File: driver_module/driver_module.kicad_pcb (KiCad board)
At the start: 4 copper layers, 68.8 x 36 mm, 119 parts, among them J1 Power Input, J19 Conn_01x03, J2 Power Input, J21 Power Input, J4 Conn_02x06_Odd_Even, J5 Conn_02x06_Odd_Even, J6 Conn_01x06, Q1 Q_PNP_BEC, Q2 Q_PNP_BEC, Q3 Q_PNP_BEC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

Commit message: First pass responding to design review. Copper changes done but final review not complete.
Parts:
- removed the G*** at (144.9, 72.0)
- removed the G*** at (141.1, 59.7)
- removed the G*** at (142.9, 48.8)
- added C5: 2.2uF 100V, Capacitor_SMD:C_0805_2012Metric, B.Cu at (118.8, 102.9)
- added C7: DNP, Capacitor_SMD:C_0603_1608Metric, B.Cu at (119.0, 96.7)
- added C8: 4.7uF 35V, Capacitor_SMD:C_0603_1608Metric, B.Cu at (116.3, 102.8)
- added R10: R, Capacitor_SMD:C_0603_1608Metric, B.Cu at (115.7, 96.7)
- added R6: R, Capacitor_SMD:C_0603_1608Metric, B.Cu at (114.9, 102.7)
- added U3: TPS7A1601DGNT, parts:DGN0008C_N, B.Cu at (117.4, 99.4)
- moved J19 1.00 mm to (124.7, 100.0)
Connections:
- J4 pad 1: VMOT -> GND
- J4 pad 2: GND -> VMOT
- J4 pad 3: VMOT -> /M2A_P
- J4 pad 4: /M2A_P -> VMOT
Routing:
- net +12V: track 90.2 -> 126.9 mm, vias 0 -> 1
- net GND: track 75.1 -> 90.1 mm, vias 141 -> 136
- net VMOT: track 43.2 -> 52.6 mm
- net Net-(U3-FB): track 0.00 -> 6.95 mm
- net Net-(U3-DELAY): track 0.00 -> 4.33 mm
- net /M2A_P: track 34.0 -> 35.9 mm
- removed copper zone on F.Cu, net (none)
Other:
- board text removed: "0"
- board text removed: "1"
- board text removed: "A1"
- board text removed: "A2"
- board text removed: "ADC1"
- board text removed: "AUX1"
- board text removed: "AUX2"
- board text removed: "B1"
- board text removed: "B2"
- board text removed: "BOOT1"
- board text removed: "BOOT2"
- board text removed: "C"
- board text removed: "C1"
- board text removed: "C2"
- board text removed: "CAN INPUT"
- board text removed: "CAN OUTPUT"
- board text removed: "CAN2"
- board text removed: "CPU1/MOT"
- board text removed: "CPU2/AUX"
- board text removed: "Debug1"
- board text removed: "Debug2"
- board text removed: "Dual RP2040 BLDC Driver"
- board text removed: "ENA"
- board text removed: "ESTOP"
- board text removed: "PWR"
- board text removed: "Profile"
- board text removed: "REMOTE"
- board text removed: "RX"
- board text removed: "TX"
- board text removed: "USB1"
- board text removed: "USB2"
- board text removed: "on"

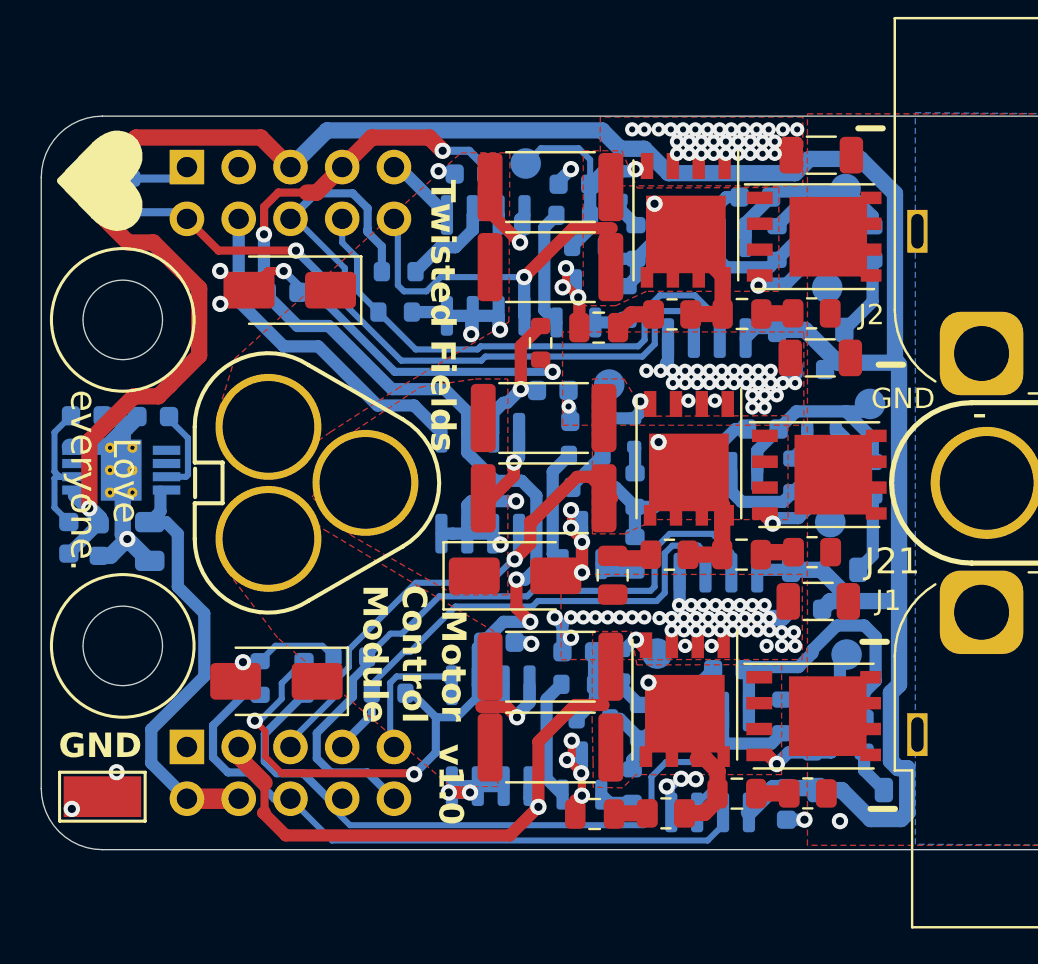
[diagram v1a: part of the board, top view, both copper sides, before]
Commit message: Clean up of motor, base, and UI PCBs. Could be ready to order.
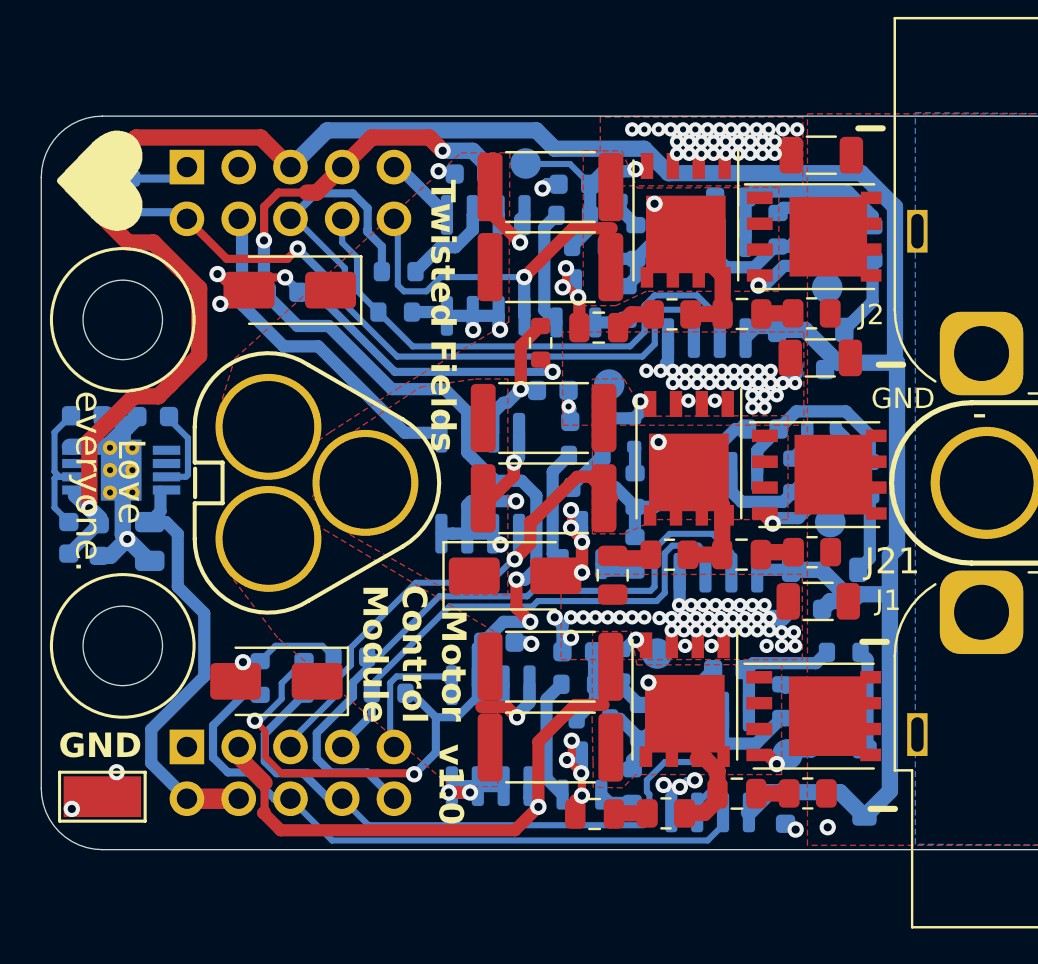
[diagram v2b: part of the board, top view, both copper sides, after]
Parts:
- removed TP62, TP78: TestPoint, parts:TestPoint_Pad_D1.5mm_no_courtyard
- C3, C6: value 150uF 63V solid -> 220uF 63V solid
- moved TP73 5.69 mm to (150.1, 113.3)
- moved R3 4.17 mm to (152.9, 108.3), turned to 180 degrees
- moved R33 1.21 mm to (152.2, 111.5), turned to 0 degrees
- moved C65 1.20 mm to (147.3, 86.0)
- moved D7 0.78 mm to (153.9, 114.7), turned to -90 degrees
- moved R31 0.75 mm to (149.8, 110.7)
- moved R8 0.65 mm to (149.7, 87.6)
- moved C15 0.21 mm to (150.0, 116.0)
- moved R26 0.15 mm to (154.2, 99.8)
- moved D17 0.11 mm to (151.9, 110.0)
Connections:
- net /M2A_N renamed /A_N
- net /M2A_P renamed /A_P
- net /M2B_N renamed /B_N
- net /M2B_P renamed /B_P
- net /M2C_N renamed /C_N
- net /M2C_P renamed /C_P
- net M2A_PWM_H renamed A_PWM_H
- net M2A_PWM_L\ renamed A_PWM_L\
- net M2A_SENSE renamed A_SENSE
- net M2B_PWM_H renamed B_PWM_H
- net M2B_PWM_L\ renamed B_PWM_L\
- net M2B_SENSE renamed B_SENSE
- net M2C_PWM_H renamed C_PWM_H
- net M2C_PWM_L\ renamed C_PWM_L\
- net M2C_SENSE renamed C_SENSE
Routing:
- net Net-(U8-VB): track 13.8 -> 6.30 mm
- net +12V: track 126.9 -> 123.3 mm
- net Net-(D7-K): track 2.29 -> 4.96 mm
- net /2AGH: track 9.04 -> 6.98 mm
- net Net-(U5-VB): track 10.6 -> 9.16 mm
- net /2CGL: track 11.5 -> 10.2 mm
- net GND: track 90.1 -> 88.8 mm
- net /C_P: track 29.8 -> 28.7 mm
- net A_PWM_L\: track 33.1 -> 32.5 mm
- net Net-(U2-VB): track 8.69 -> 9.29 mm
- net /TH1_SENSE: track 26.0 -> 26.5 mm
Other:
- board text added: "A"
- board text added: "B"
- board text added: "C"
- board text added: "H"
- board text added: "L"

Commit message: Respond to latest round of design review.
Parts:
- added D1: SMAJ51A, Diode_SMD:D_SMC, B.Cu at (163.2, 112.1)
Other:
- board text added: "github.com/ Twisted-Fields/rp2040-motor-controller"
- board text removed: "github.com/ Twisted-Fields/ rp2040-motor-controller"
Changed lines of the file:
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@@
     )
   )
+  (footprint "Diode_SMD:D_SMC" (layer "B.Cu")
+    (at 163.22 112.125 180)
+    (descr "Diode SMC (DO-214AB)")
+    (tags "Diode SMC (DO-214AB)")
+    (property "LCSC" "C438169")
+    (property "Sheetfile" "driver_module.kicad_sch")
+    (property "Sheetname" "")
+    (property "ki_description" "200W unidirectional Transil Transient Voltage Suppressor, 54Vrwm, SMF")
+    (property "ki_keywords" "diode TVS voltage suppressor")
+    (attr smd)
+    (fp_text reference "D1" (at 0 4.1) (layer "B.SilkS") hide
+        (effects (font (size 1 1) (thickness 0.15)) (justify mirror))
+    )
+    (fp_text value "SMAJ51A" (at 0 -4.2) (layer "B.Fab")
+        (effects (font (size 1 1) (thickness 0.15)) (justify mirror))
+    )
+    (fp_text user "${REFERENCE}" (at 0 1.9) (layer "B.Fab")
+        (effects (font (size 1 1) (thickness 0.15)) (justify mirror))
+    )
+    (fp_line (start -4.91 -3.25) (end -4.91 3.25)
+      (stroke (width 0.12) (type solid)) (layer "B.SilkS"))
+    (fp_line (start -4.91 -3.25) (end 3.6 -3.25)
+      (stroke (width 0.12) (type solid)) (layer "B.SilkS"))
+    (fp_line (start -4.91 3.25) (end 3.6 3.25)
+      (stroke (width 0.12) (type solid)) (layer "B.SilkS"))
+    (fp_line (start -4.9 -3.35) (end -4.9 3.35)
+      (stroke (width 0.05) (type solid)) (layer "B.CrtYd"))
+    (fp_line (start -4.9 3.35) (end 4.9 3.35)
+      (stroke (width 0.05) (type solid)) (layer "B.CrtYd"))
+    (fp_line (start 4.9 -3.35) (end -4.9 -3.35)
+      (stroke (width 0.05) (type solid)) (layer "B.CrtYd"))
+    (fp_line (start 4.9 3.35) (end 4.9 -3.35)
+      (stroke (width 0.05) (type solid)) (layer "B.CrtYd"))
+    (fp_line (start -3.55 -3.1) (end -3.55 3.1)
+      (stroke (width 0.1) (type solid)) (layer "B.Fab"))
+    (fp_line (start -0.64944 -0.00102) (end -1.55114 -0.00102)
+      (stroke (width 0.1) (type solid)) (layer "B.Fab"))
+    (fp_line (start -0.64944 -0.00102) (end 0.50118 -0.75032)
+      (stroke (width 0.1) (type solid)) (layer "B.Fab"))
+    (fp_line (start -0.64944 -0.00102) (end 0.50118 0.79908)
+      (stroke (width 0.1) (type solid)) (layer "B.Fab"))
+    (fp_line (start -0.64944 0.79908) (end -0.64944 -0.80112)
+      (stroke (width 0.1) (type solid)) (layer "B.Fab"))
+    (fp_line (start 0.50118 -0.75032) (end 0.50118 0.79908)
+      (stroke (width 0.1) (type solid)) (layer "B.Fab"))
+    (fp_line (start 0.50118 -0.00102) (end 1.4994 -0.00102)
+      (stroke (width 0.1) (type solid)) (layer "B.Fab"))
+    (fp_line (start 3.55 -3.1) (end -3.55 -3.1)
+      (stroke (width 0.1) (type solid)) (layer "B.Fab"))
+    (fp_line (start 3.55 3.1) (end -3.55 3.1)
+      (stroke (width 0.1) (type solid)) (layer "B.Fab"))
+    (fp_line (start 3.55 3.1) (end 3.55 -3.1)
+      (stroke (width 0.1) (type solid)) (layer "B.Fab"))
+    (pad "1" smd roundrect (at -3.4 0 90) (size 3.3 2.5) (layers "B.Cu" "B.Paste" "B.Mask") (roundrect_rratio 0.1)
+      (net 4 "VMOT") (pinfunction "A1") (pintype "passive"))
+    (pad "2" smd roundrect (at 3.4 0 90) (size 3.3 2.5) (layers "B.Cu" "B.Paste" "B.Mask") (roundrect_rratio 0.1)
+      (net 1 "GND") (pinfunction "A2") (pintype "passive"))
+    (model "${KICAD6_3DMODEL_DIR}/Diode_SMD.3dshapes/D_SMC.wrl"
+      (offset (xyz 0 0 0))
+      (scale (xyz 1 1 1))
+      (rotate (xyz 0 0 0))
+    )
+  )
   (footprint "Resistor_SMD:R_0603_1608Metric" (layer "B.Cu")
     (at 142.251268 91.17005 -90)
@@
         (effects (font (size 1 1) (thickness 0.15)) (justify mirror))
     )
+    (fp_text user "${REFERENCE}" (at -1.5 2.75 180 unlocked) (layer "B.SilkS")
+        (effects (font (size 1 1) (thickness 0.15)) (justify mirror))
+    )
     (fp_poly
       (pts
@@
     (effects (font (size 1 1) (thickness 0.15)) (justify mirror))
   )
-  (gr_text "      github.com/\n      Twisted-Fields/\nrp2040-motor-controller" (at 165.8 114.45) (layer "B.SilkS")
-    (effects (font (size 1 1) (thickness 0.2)) (justify mirror))
+  (gr_text "github.com/\nTwisted-Fields/rp2040-motor-controller" (at 180.8 115.95) (layer "B.SilkS")
+    (effects (font (size 0.8 0.8) (thickness 0.2)) (justify left mirror))
   )
   (gr_text "GND" (at 394.775 92.1) (layer "B.SilkS")

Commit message: Update boards for latest build, pending design review.
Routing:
- net +12V: track 123.3 -> 120.5 mm

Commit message: Change enable behavior and ensure low side FETs activate for hardware braking
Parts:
- removed G***: LOGO, taylor_footprints:twisted_2
- removed G***: LOGO, taylor_footprints:twisted_icon
- removed G***: LOGO, taylor_footprints:twisted
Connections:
- R119 pad 1: +3V3 -> GND
- R122 pad 1: +3V3 -> GND
- R124 pad 1: +3V3 -> GND
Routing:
- net +3V3: track 87.7 -> 61.7 mm, vias 7 -> 5
- net GND: track 88.8 -> 98.5 mm
- net /C_P: track 28.7 -> 26.4 mm
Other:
- board text added: "Love"
- board text added: "everyone."
- board text removed: "5V ISO"
- board text removed: "Designed by Sequoia Sempervirens For Twisted Fields"
- board text removed: "Dual CPU Version 3.2"
- board text removed: "ENC1"
- board text removed: "ENC2"
- board text removed: "Enc1 Filt"
- board text removed: "Enc2 Filt"
- board text removed: "GND ISO"
- board text removed: "Love everyone."
- board text removed: "Please clone this board!"
- board text removed: "RP2040 Brushless Motor Controller"
- board text removed: "The smallest change can be the beginning of something big."
- board text removed: "VMOT"
- board text removed: "We are all star stuff."
- board text removed: "We need your help. Fork the design and make it yours."
- board text removed: "You can do it!"

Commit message: Updated files for boards ordered July 2024
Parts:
- D1: value SMAJ51A -> SMDJ51CA
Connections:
- U3 pad 5: unconnected-(U3-EN-Pad5) -> VMOT
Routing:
- net VMOT: track 52.1 -> 56.7 mm, vias 1 -> 3
- net Net-(U3-DELAY): track 4.33 -> 5.13 mm
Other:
- board text added: "Design by Sequoia Hope Alexander"
- board text added: "v1.1"
- board text removed: "Design by Sequoia Sempervirens"
- board text removed: "v1.0"
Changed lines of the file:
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@@
 	(net 56 "C_SENSE")
 	(net 57 "unconnected-(U3-PG-Pad3)")
-	(net 58 "unconnected-(U3-EN-Pad5)")
-	(net 59 "unconnected-(U3-NC-Pad6)")
-	(net 60 "Net-(U3-DELAY)")
-	(net 61 "Net-(U3-FB)")
+	(net 58 "unconnected-(U3-NC-Pad6)")
+	(net 59 "Net-(U3-DELAY)")
+	(net 60 "Net-(U3-FB)")
 	(footprint "RP2040_minimal:MountingHole_3.9mm_Plastite_#6"
 		(layer "F.Cu")
@@
 			)
 		)
-		(property "Datasheet" ""
+		(property "Datasheet" "https://wmsc.lcsc.com/wmsc/upload/file/pdf/v2/lcsc/2305121702_NJCON-2210631013R00_C5455531.pdf"
 			(at 0 0 0)
 			(unlocked yes)
@@
 			)
 		)
-		(property "LCSC" "C2983797"
+		(property "LCSC" "C5455531"
+			(at 0 0 0)
+			(layer "F.Fab")
+			(hide yes)
+			(effects
+				(font
+					(size 1 1)
+					(thickness 0.15)
+				)
+			)
+		)
+		(property "MPN" "2210631013R00"
 			(at 0 0 0)
+			(unlocked yes)
 			(layer "F.Fab")
 			(hide yes)
@@
 			)
 		)
-		(property "Datasheet" ""
+		(property "Datasheet" "https://wmsc.lcsc.com/wmsc/upload/file/pdf/v2/lcsc/2305121702_NJCON-2210631013R00_C5455531.pdf"
 			(at 0 0 0)
 			(unlocked yes)
@@
 			)
 		)
-		(property "LCSC" "C2983797"
+		(property "LCSC" "C5455531"
+			(at 0 0 0)
+			(layer "F.Fab")
+			(hide yes)
+			(effects
+				(font
+					(size 1 1)
+					(thickness 0.15)
+				)
+			)
+		)
+		(property "MPN" "2210631013R00"
 			(at 0 0 0)
+			(unlocked yes)
 			(layer "F.Fab")
 			(hide yes)
@@
 			(layers "B.Cu" "B.Paste" "B.Mask")
 			(roundrect_rratio 0.25)
-			(net 61 "Net-(U3-FB)")
+			(net 60 "Net-(U3-FB)")
 			(pintype "passive")
 		)
@@
 			(layers "B.Cu" "B.Paste" "B.Mask")
 			(roundrect_rratio 0.25)
-			(net 60 "Net-(U3-DELAY)")
+			(net 59 "Net-(U3-DELAY)")
 			(pintype "passive")
 		)
@@
 			)
 		)
-		(property "Value" "SMAJ51A"
+		(property "Value" "SMDJ51CA"
 			(at 0 -4.2 0)
 			(layer "B.Fab")
@@
 			)
 		)
-		(property "LCSC" "C438169"
+		(property "LCSC" "C406702"
 			(at 0 0 0)
 			(layer "B.Fab")
@@
 			(layers "B.Cu" "B.Paste" "B.Mask")
 			(roundrect_rratio 0.25)
-			(net 61 "Net-(U3-FB)")
+			(net 60 "Net-(U3-FB)")
 			(pintype "passive")
 		)
@@
 		(fp_arc
 			(start 1.375443 -1.501336)
-			(mid 1.462506 -1.464167)
+			(mid 1.46252 -1.464181)
 			(end 1.499675 -1.377104)
 			(stroke
@@
 		(fp_arc
 			(start 1.499675 1.371582)
-			(mid 1.462492 1.458621)
+			(mid 1.462487 1.458626)
 			(end 1.375443 1.495814)
 			(stroke
@@
 			(size 0.449999 1.35)
 			(layers "B.Cu" "B.Paste" "B.Mask")
-			(net 61 "Net-(U3-FB)")
+			(net 60 "Net-(U3-FB)")
 			(pinfunction "FB")
 			(pintype "input")
@@
 			(net 57 "unconnected-(U3-PG-Pad3)")
 			(pinfunction "PG")
-			(pintype "open_collector")
+			(pintype "open_collector+no_connect")
 		)
 		(pad "4" smd rect
@@
 			(size 0.449999 1.35)
 			(layers "B.Cu" "B.Paste" "B.Mask")
-			(net 58 "unconnected-(U3-EN-Pad5)")
+			(net 4 "VMOT")
 			(pinfunction "EN")
 			(pintype "input")
@@
 			(size 0.449999 1.35)
 			(layers "B.Cu" "B.Paste" "B.Mask")
-			(net 59 "unconnected-(U3-NC-Pad6)")
+			(net 58 "unconnected-(U3-NC-Pad6)")
 			(pinfunction "NC")
-			(pintype "unspecified")
+			(pintype "unspecified+no_connect")
 		)
 		(pad "7" smd rect
@@
 			(size 0.449999 1.35)
 			(layers "B.Cu" "B.Paste" "B.Mask")
-			(net 60 "Net-(U3-DELAY)")
+			(net 59 "Net-(U3-DELAY)")
 			(pinfunction "DELAY")
 			(pintype "unspecified")
@@
 		(layer "Edge.Cuts")
 	)
-	(gr_text "Design by\nSequoia\nSempervirens"
-		(at 173.65 108.4 0)
+	(gr_text "Design by\nSequoia Hope\nAlexander"
+		(at 174.85 109.05 0)
 		(layer "B.SilkS")
 		(effects
@@
 		)
 	)
-	(gr_text "v1.0"
+	(gr_text "v1.1"
 		(at 133.6 114.8 270)
 		(layer "F.SilkS")
@@
 	)
 	(segment
+		(start 120.15 100.9)
+		(end 120.25 100.8)
+		(width 0.2)
+		(layer "F.Cu")
+		(net 4)
+	)
+	(segment
 		(start 120.65 115.5)
 		(end 123.19 115.5)
@@
 		(net 4)
 	)
+	(segment
+		(start 120.25 100.8)
+		(end 120.25 98)
+		(width 0.2)
+		(layer "F.Cu")
+		(net 4)
+	)
 	(via
-		(at 152.1 116.9)
+		(at 120.15 100.9)
 		(size 0.8)
 		(drill 0.4)
 		(layers "F.Cu" "B.Cu")
+		(net 4)
+	)
+	(via
+		(at 152.35 114.55)
+		(size 1)
+		(drill 0.6)
+		(layers "F.Cu" "B.Cu")
 		(free yes)
 		(net 4)
 	)
-	(segment
-		(start 150.72995 115.52995)
-		(end 152.1 116.9)
-		(width 0.8)
-		(layer "In1.Cu")
+	(via
+		(at 120.25 98)
+		(size 0.8)
+		(drill 0.4)
+		(layers "F.Cu" "B.Cu")
 		(net 4)
 	)
 	(segment
-		(start 148.5 117.25)
-		(end 150.22005 115.52995)
+		(start 151.2 114.55)
+		(end 148.5 117.25)
 		(width 0.8)
 		(layer "In1.Cu")
@@
 	(segment
 		(start 124.94 117.25)
-		(end 148.5 117.25)
+		(end 123.19 115.5)
 		(width 0.8)
 		(layer "In1.Cu")
@@
 	)
 	(segment
-		(start 150.22005 115.52995)
-		(end 150.72995 115.52995)
+		(start 152.35 114.55)
+		(end 151.2 114.55)
 		(width 0.8)
 		(layer "In1.Cu")
@@
 	)
 	(segment
-		(start 123.19 115.5)
+		(start 148.5 117.25)
 		(end 124.94 117.25)
 		(width 0.8)
@@
 	)
 	(segment
+		(start 119.850001 98.399999)
+		(end 120.25 98)
+		(width 0.2)
+		(layer "B.Cu")
+		(net 4)
+	)
+	(segment
+		(start 120.15 100.9)
+		(end 120.15 100.849997)
+		(width 0.2)
+		(layer "B.Cu")
+		(net 4)
+	)
+	(segment
 		(start 121.5 106.4)
 		(end 121.5 109.5)
@@
 	)
 	(segment
+		(start 119.650003 98.399999)
+		(end 119.850001 98.399999)
+		(width 0.2)
+		(layer "B.Cu")
+		(net 4)
+	)
+	(segment
+		(start 120.15 100.849997)
+		(end 119.650003 100.35)
+		(width 0.2)
+		(layer "B.Cu")
+		(net 4)
+	)
+	(segment
 		(start 119.625 101.925)
 		(end 120.2 102.5)
@@
 	)
 	(segment
+		(start 153.780895 116.5)
+		(end 153.904627 116.376268)
+		(width 0.8)
+		(layer "B.Cu")
+		(net 53)
+	)
+	(segment
 		(start 154.983732 105.466268)
 		(end 155.15 105.3)
@@
 	)
 	(segment
+		(start 152.2 116.5)
+		(end 153.780895 116.5)
+		(width 0.8)
+		(layer "B.Cu")
+		(net 53)
+	)
+	(segment
 		(start 155.5 94.1)
 		(end 152.6 94.1)
@@
 	)
 	(segment
+		(start 150.87995 115.17995)
+		(end 152.2 116.5)
+		(width 0.8)
+		(layer "B.Cu")
+		(net 53)
+	)
+	(segment
 		(start 155.15 103.55)
 		(end 155.5 103.2)
@@
 	)
 	(segment
+		(start 150.028411 115.17995)
+		(end 150.87995 115.17995)
+		(width 0.8)
+		(layer "B.Cu")
+		(net 53)
+	)
+	(segment
 		(start 115.8575 101.2425)
 		(end 115.215 100.6)
@@
 	)
 	(segment
-		(start 150.028411 115.17995)
-		(end 152.708309 115.17995)
-		(width 0.8)
-		(layer "B.Cu")
-		(net 53)
-	)
-	(segment
 		(start 150.299628 104.266268)
 		(end 151.766268 104.266268)
@@
 	)
 	(segment
-		(start 152.708309 115.17995)
-		(end 153.904627 116.376268)
-		(width 0.8)
-		(layer "B.Cu")
-		(net 53)
-	)
-	(segment
 		(start 145.529949 92.89249)
 		(end 145.529949 91.917491)
@@
 	)
 	(segment
-		(start 120.7 97.8)
-		(end 120.7 99.6)
+		(start 121.15 99.15)
+		(end 120.600001 99.699999)
 		(width 0.3)
 		(layer "B.Cu")
-		(net 60)
+		(net 59)
 	)
 	(segment
-		(start 119.77 96.87)
-		(end 120.7 97.8)
+		(start 121.15 97.4)
+		(end 121.15 99.15)
 		(width 0.3)
 		(layer "B.Cu")
-		(net 60)
+		(net 59)
 	)
 	(segment
 		(start 119.77 96.745001)
-		(end 119.77 96.87)
+		(end 120.495001 96.745001)
 		(width 0.3)
 		(layer "B.Cu")
-		(net 60)
+		(net 59)
 	)
 	(segment
-		(start 120.7 99.6)
-		(end 120.600001 99.699999)
+		(start 120.600001 99.699999)
+		(end 119.650003 99.699999)
 		(width 0.3)
 		(layer "B.Cu")
-		(net 60)
+		(net 59)
 	)
 	(segment
-		(start 120.600001 99.699999)
-		(end 119.650003 99.699999)
+		(start 120.495001 96.745001)
+		(end 121.15 97.4)
 		(width 0.3)
 		(layer "B.Cu")
-		(net 60)
+		(net 59)
 	)
 	(segment
@@
 		(width 0.3)
 		(layer "B.Cu")
-		(net 61)
+		(net 60)
 	)
 	(segment
@@
 		(width 0.3)
 		(layer "B.Cu")
-		(net 61)
+		(net 60)
 	)
 	(segment
@@
 		(width 0.3)
 		(layer "B.Cu")
-		(net 61)
+		(net 60)
 	)
 	(segment
@@
 		(width 0.3)
 		(layer "B.Cu")
-		(net 61)
+		(net 60)
 	)
 	(segment
@@
 		(width 0.3)
 		(layer "B.Cu")
-		(net 61)
+		(net 60)
 	)
 	(segment
@@
 		(width 0.3)
 		(layer "B.Cu")
-		(net 61)
+		(net 60)
 	)
 	(segment
@@
 		(width 0.3)
 		(layer "B.Cu")
-		(net 61)
+		(net 60)
 	)
 	(segment
@@
 		(width 0.3)
 		(layer "B.Cu")
-		(net 61)
+		(net 60)
 	)
 	(zone
